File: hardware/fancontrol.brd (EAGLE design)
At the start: 55 x 50 mm, 11 parts, among them Q1 IRLZ44Z, T1 BC547

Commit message: changed R2 from 10k to 10R
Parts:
- R2: value 10k -> 10R
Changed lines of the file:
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@@
 <element name="R1" library="rcl" package="0207/7" value="10k" x="42.78" y="17.15" rot="R180"/>
 <element name="T1" library="transistor" package="TO92" value="BC547" x="28.72" y="15.42" rot="R270"/>
-<element name="R2" library="rcl" package="0207/7" value="10k" x="34" y="26" rot="R90"/>
+<element name="R2" library="rcl" package="0207/7" value="10R" x="34" y="26" rot="R90"/>
 <element name="R3" library="rcl" package="0207/7" value="10k" x="28.5" y="25.9" rot="R90"/>
 <element name="C1" library="rcl" package="E5-10,5" value="470u" x="18.53" y="17.29" rot="R270"/>

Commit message: connect JP2 to GND. Fixes #2
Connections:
- removed net N$5: JP2.3
- net GND: now also JP2.3
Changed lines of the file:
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@@
 <?xml version="1.0" encoding="utf-8"?>
 <!DOCTYPE eagle SYSTEM "eagle.dtd">
-<eagle version="6.2">
+<eagle version="6.4">
 <drawing>
 <settings>
@@
 </class>
 </classes>
-<designrules>
+<designrules name="default">
 <description language="de">&lt;b&gt;EAGLE Design Rules&lt;/b&gt;
 &lt;p&gt;
@@
 <vertex x="0" y="50"/>
 </polygon>
+<contactref element="JP2" pad="3"/>
 </signal>
 <signal name="N$3">
@@
 <wire x1="46.82" y1="17.38" x2="46.59" y2="17.15" width="0.4064" layer="16"/>
 </signal>
-<signal name="N$5">
-<contactref element="JP2" pad="3"/>
-</signal>
 </signals>

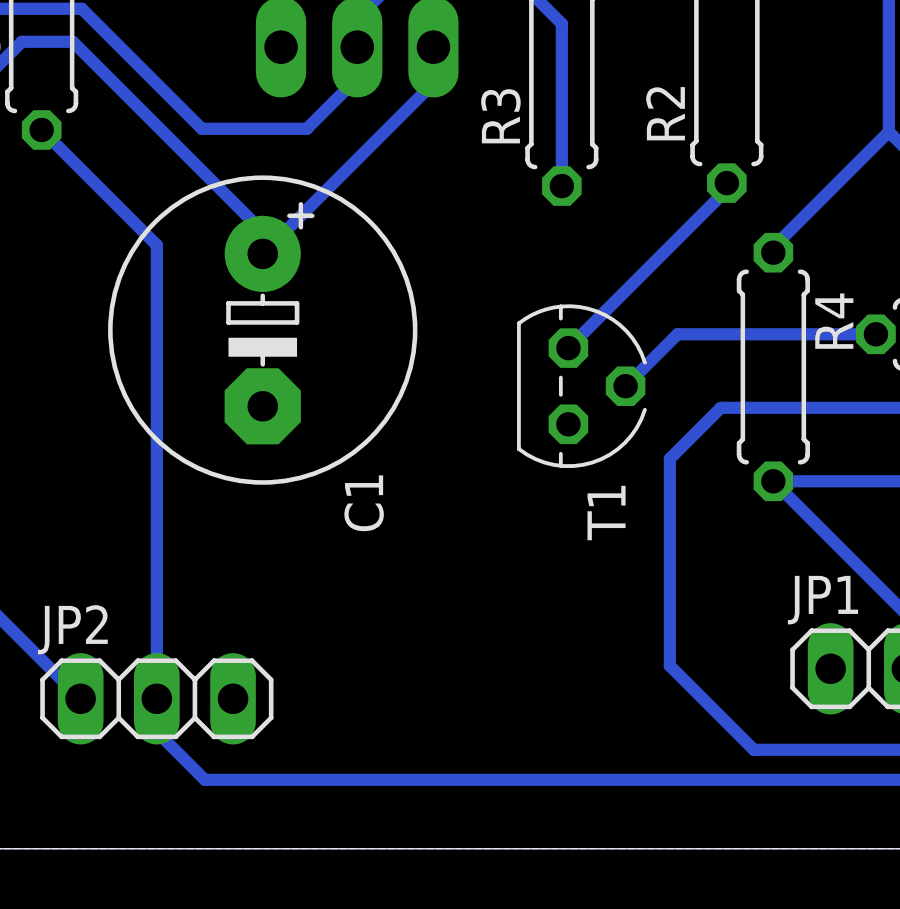
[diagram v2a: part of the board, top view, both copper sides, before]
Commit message: added capacitors to Vin. Fixes #1
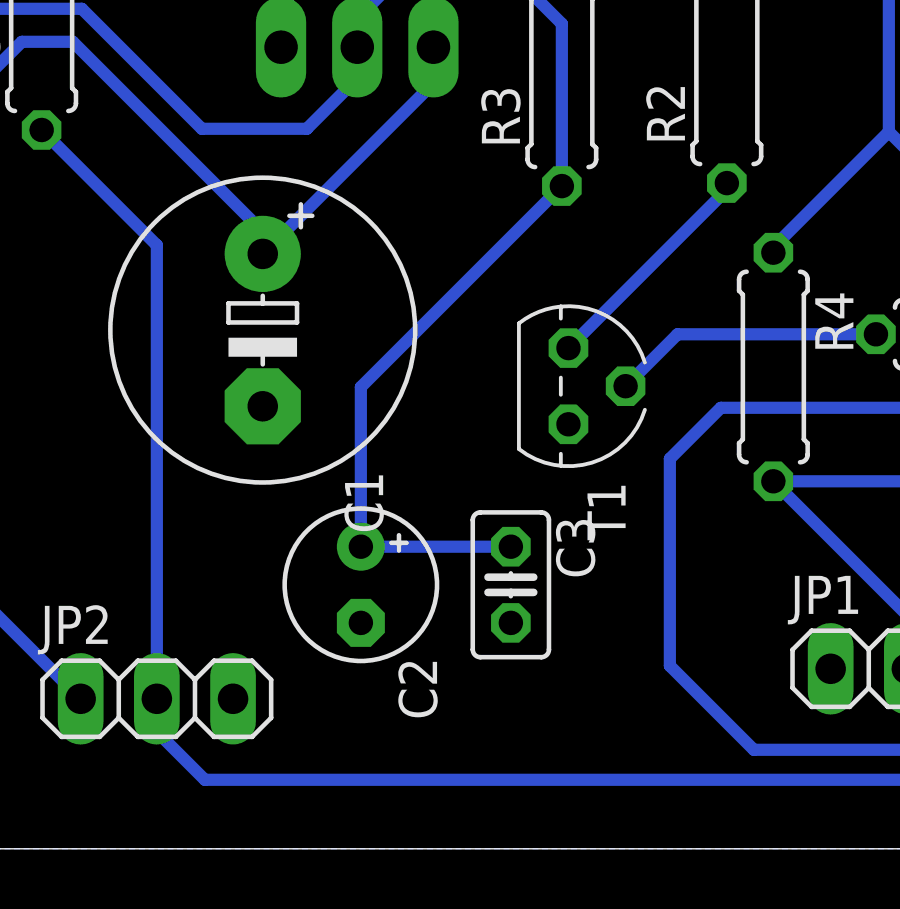
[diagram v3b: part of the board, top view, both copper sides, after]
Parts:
- added C2: 10u, rcl:E2,5-5
- added C3: 100n, rcl:C025-025X050
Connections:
- net +12V: now also C2.+, C3.1
- net GND: now also C2.-, C3.2
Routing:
- net +12V: track 39.1 -> 58.9 mm
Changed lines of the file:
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@@
 <element name="JP2" library="pinhead" package="1X03" value="" x="15" y="5"/>
 <element name="R5" library="rcl" package="0207/7" value="10k" x="11.16" y="27.77" rot="R90"/>
+<element name="C2" library="rcl" package="E2,5-5" value="10u" x="21.8" y="8.8" rot="R270"/>
+<element name="C3" library="rcl" package="C025-025X050" value="100n" x="26.8" y="8.8" rot="R270"/>
 </elements>
 <signals>
@@
 </polygon>
 <contactref element="JP2" pad="3"/>
+<contactref element="C2" pad="-"/>
+<contactref element="C3" pad="2"/>
 </signal>
 <signal name="N$3">
@@
 <wire x1="6.7" y1="26.3" x2="8.4" y2="28" width="0.4064" layer="16"/>
 <wire x1="8.4" y1="28" x2="12.5" y2="28" width="0.4064" layer="16"/>
+<contactref element="C2" pad="+"/>
+<contactref element="C3" pad="1"/>
+<wire x1="28.5" y1="22.09" x2="21.8" y2="15.39" width="0.4064" layer="16"/>
+<wire x1="21.8" y1="15.39" x2="21.8" y2="10.07" width="0.4064" layer="16"/>
+<wire x1="21.8" y1="10.07" x2="26.8" y2="10.07" width="0.4064" layer="16"/>
 </signal>
 <signal name="FAN+">

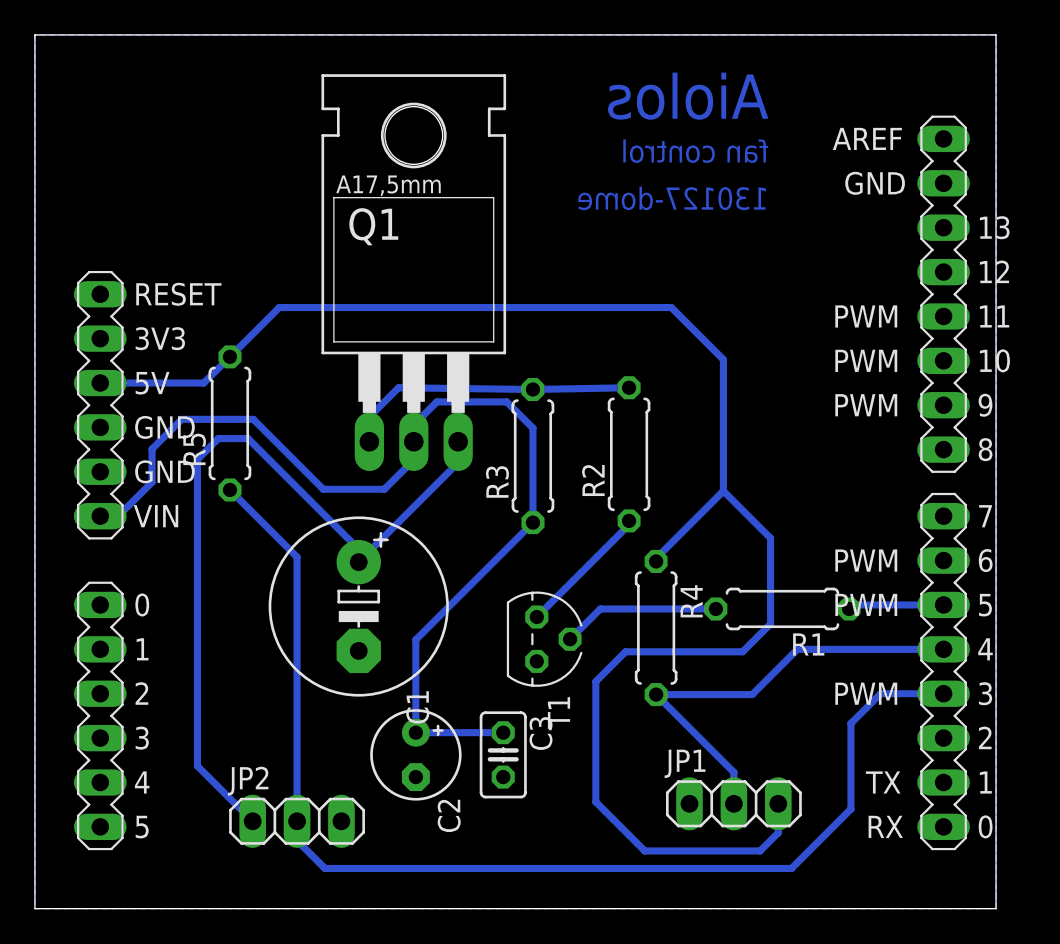
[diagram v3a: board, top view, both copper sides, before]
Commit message: Replace transistor, make routes wider
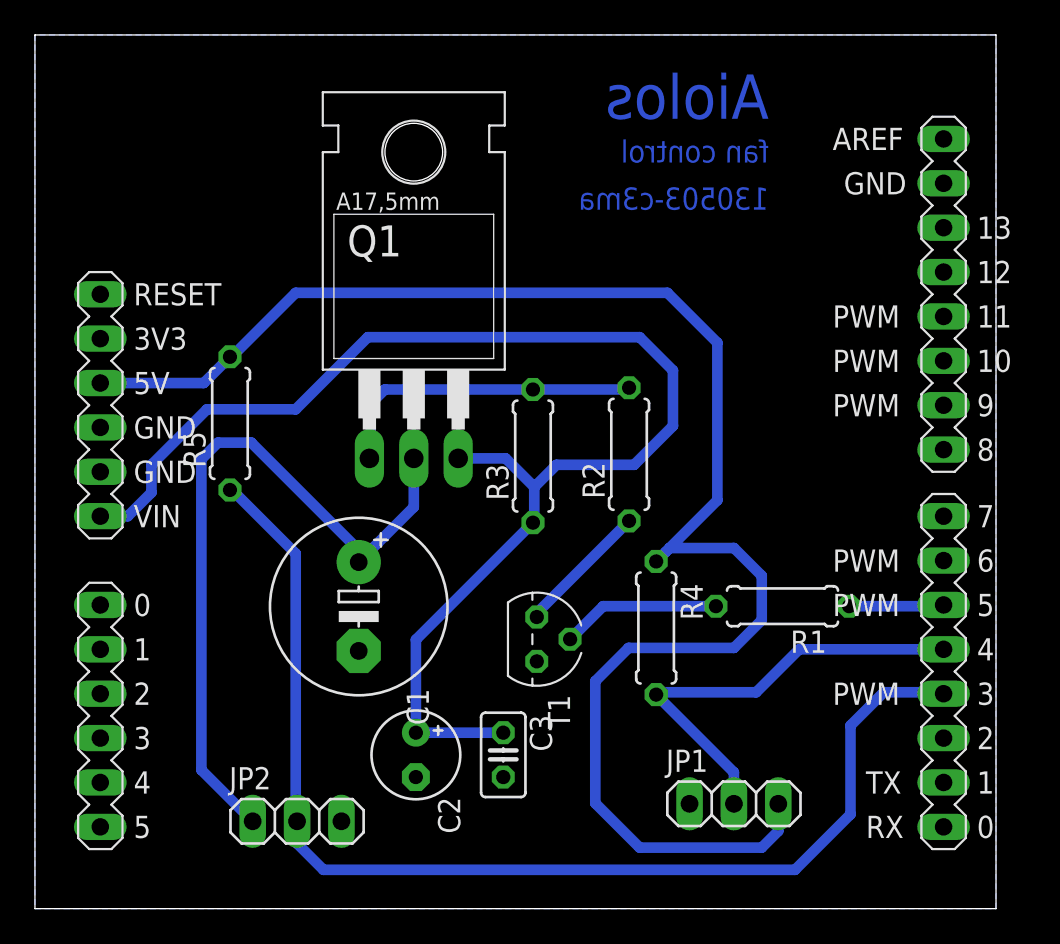
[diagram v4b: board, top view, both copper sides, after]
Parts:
- Q1: value IRLZ44Z -> BUZ171; device transistor-power:TO220BH -> transistor-fet:TO220
- moved Q1 0.95 mm to (21.7, 32.1)
- moved R1 0.16 mm to (42.8, 17.3)
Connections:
- net +12V: now also Q1.3; no longer Q1.D
- net FAN+: now also Q1.2; no longer Q1.S
- net N$3: now also Q1.1; no longer Q1.G
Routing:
- net +12V: track 58.9 -> 78.2 mm
- net FAN+: track 44.3 -> 41.8 mm
- net N$3: track 17.0 -> 18.3 mm
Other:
- board text added: "130503-c3ma"
- board text removed: "130127-dome"

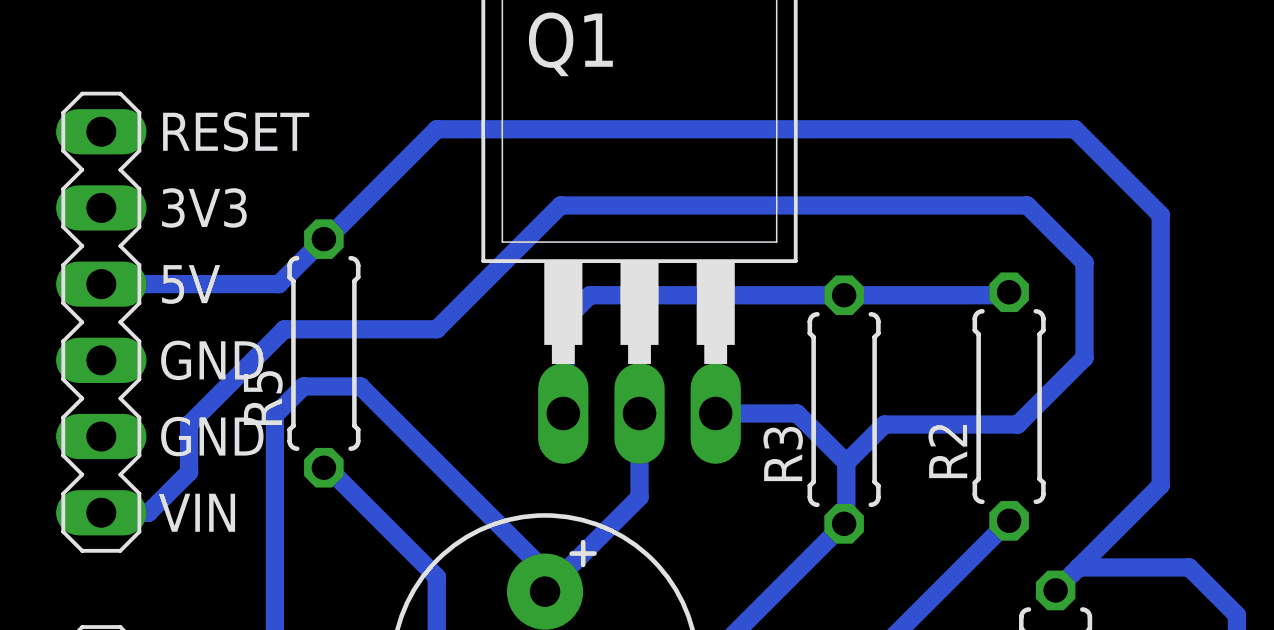
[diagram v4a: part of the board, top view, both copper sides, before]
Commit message: Fix one wire to make GND work again
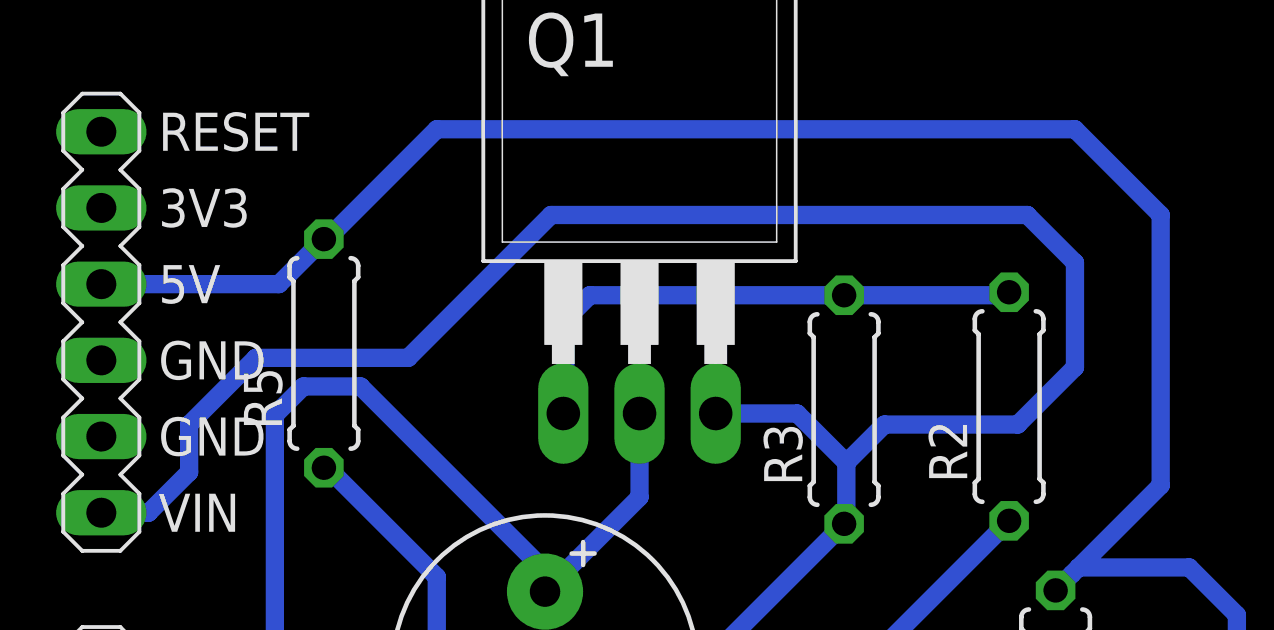
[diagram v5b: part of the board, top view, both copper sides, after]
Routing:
- net +12V: track 78.2 -> 77.5 mm
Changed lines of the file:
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@@
 <contactref element="C2" pad="-"/>
 <contactref element="C3" pad="2"/>
-<wire x1="26.8" y1="7.53" x2="37.46" y2="6" width="0" layer="19" extent="1-1"/>
 </signal>
 <signal name="+12V">
@@
 <wire x1="5.315" y1="22.46" x2="6.6675" y2="23.8125" width="0.6096" layer="16"/>
 <wire x1="6.6675" y1="23.8125" x2="6.6675" y2="25.4" width="0.6096" layer="16"/>
-<wire x1="6.6675" y1="25.4" x2="9.8425" y2="28.575" width="0.6096" layer="16"/>
-<wire x1="9.8425" y1="28.575" x2="14.9225" y2="28.575" width="0.6096" layer="16"/>
-<wire x1="14.9225" y1="28.575" x2="19.05" y2="32.7025" width="0.6096" layer="16"/>
-<wire x1="19.05" y1="32.7025" x2="34.6075" y2="32.7025" width="0.6096" layer="16"/>
-<wire x1="34.6075" y1="32.7025" x2="36.5125" y2="30.7975" width="0.6096" layer="16"/>
-<wire x1="36.5125" y1="30.7975" x2="36.5125" y2="27.6225" width="0.6096" layer="16"/>
-<wire x1="36.5125" y1="27.6225" x2="34.29" y2="25.4" width="0.6096" layer="16"/>
+<wire x1="6.6675" y1="25.4" x2="8.89" y2="27.6225" width="0.6096" layer="16"/>
+<wire x1="8.89" y1="27.6225" x2="13.97" y2="27.6225" width="0.6096" layer="16"/>
+<wire x1="13.97" y1="27.6225" x2="18.7325" y2="32.385" width="0.6096" layer="16"/>
+<wire x1="18.7325" y1="32.385" x2="34.6075" y2="32.385" width="0.6096" layer="16"/>
+<wire x1="34.6075" y1="32.385" x2="36.195" y2="30.7975" width="0.6096" layer="16"/>
+<wire x1="36.195" y1="30.7975" x2="36.195" y2="27.305" width="0.6096" layer="16"/>
+<wire x1="36.195" y1="27.305" x2="34.29" y2="25.4" width="0.6096" layer="16"/>
 <wire x1="34.29" y1="25.4" x2="29.845" y2="25.4" width="0.6096" layer="16"/>
 <wire x1="29.845" y1="25.4" x2="28.575" y2="24.13" width="0.6096" layer="16"/>
